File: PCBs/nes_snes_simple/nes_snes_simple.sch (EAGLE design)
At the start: 23 parts, among them IC1 74245

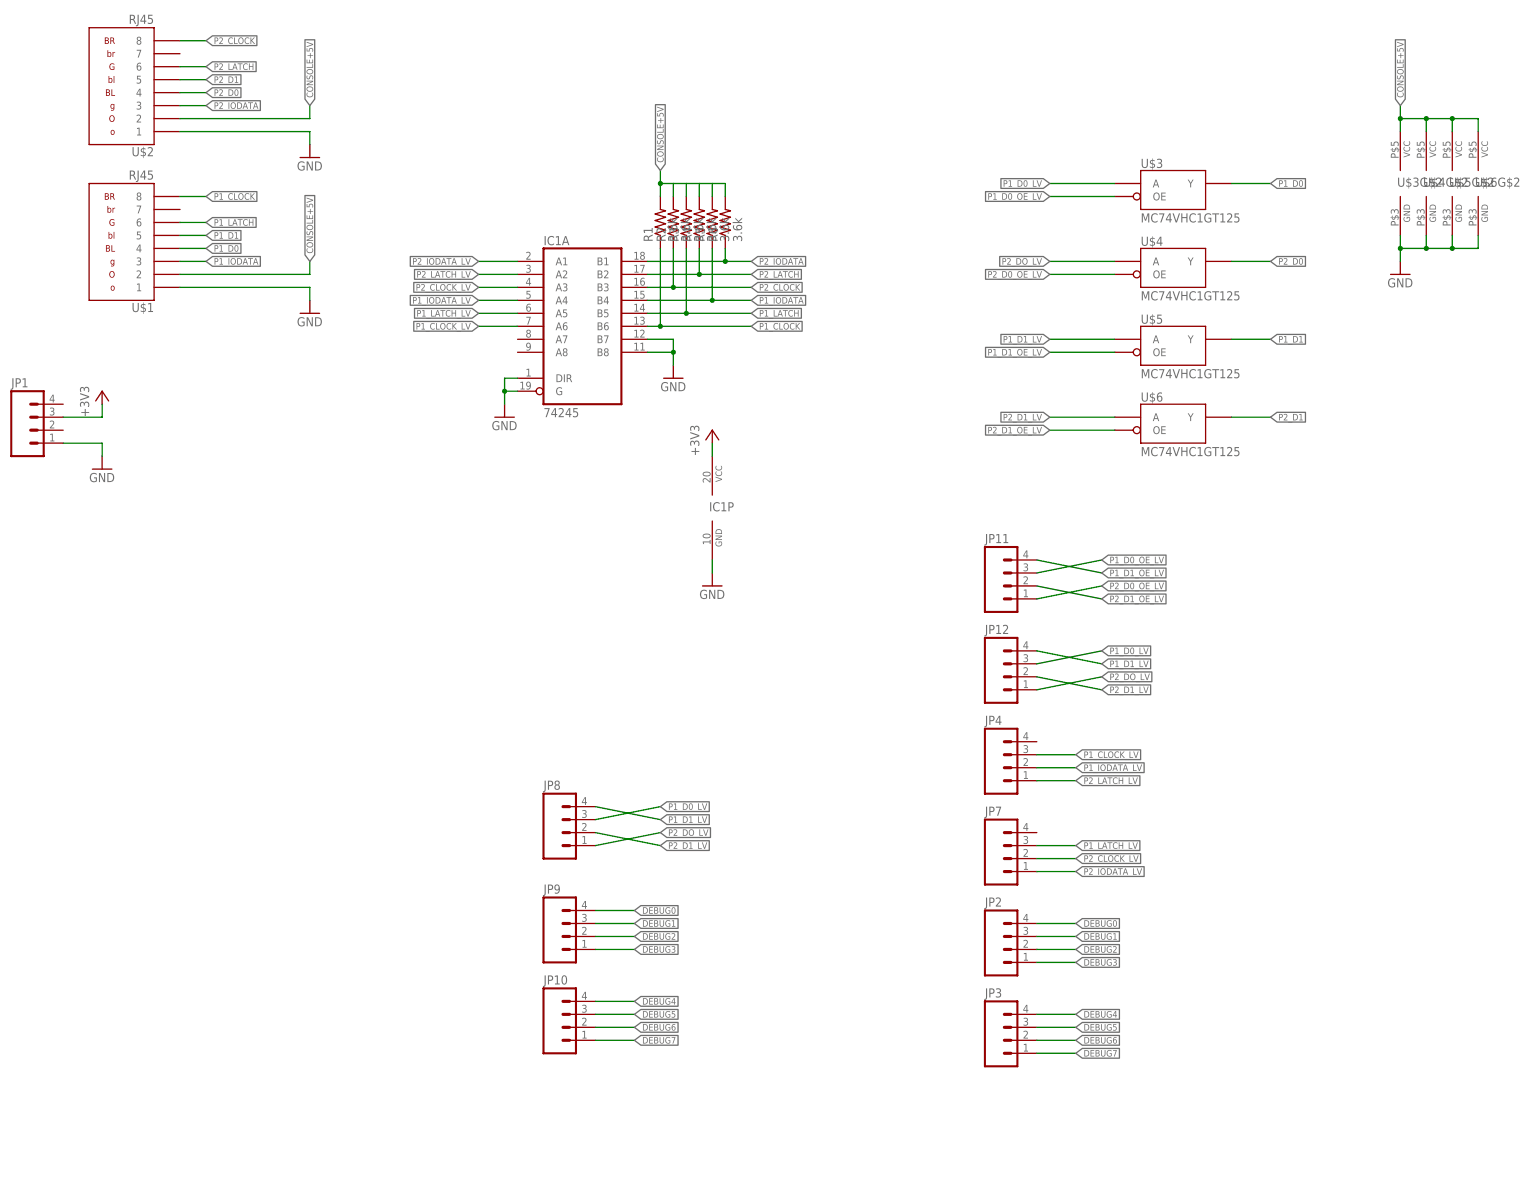
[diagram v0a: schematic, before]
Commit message: Added a tap for all the 5v lines from the console. Fixed part labels. Added more labeling. Added a logo. Cleaned up the schematic.
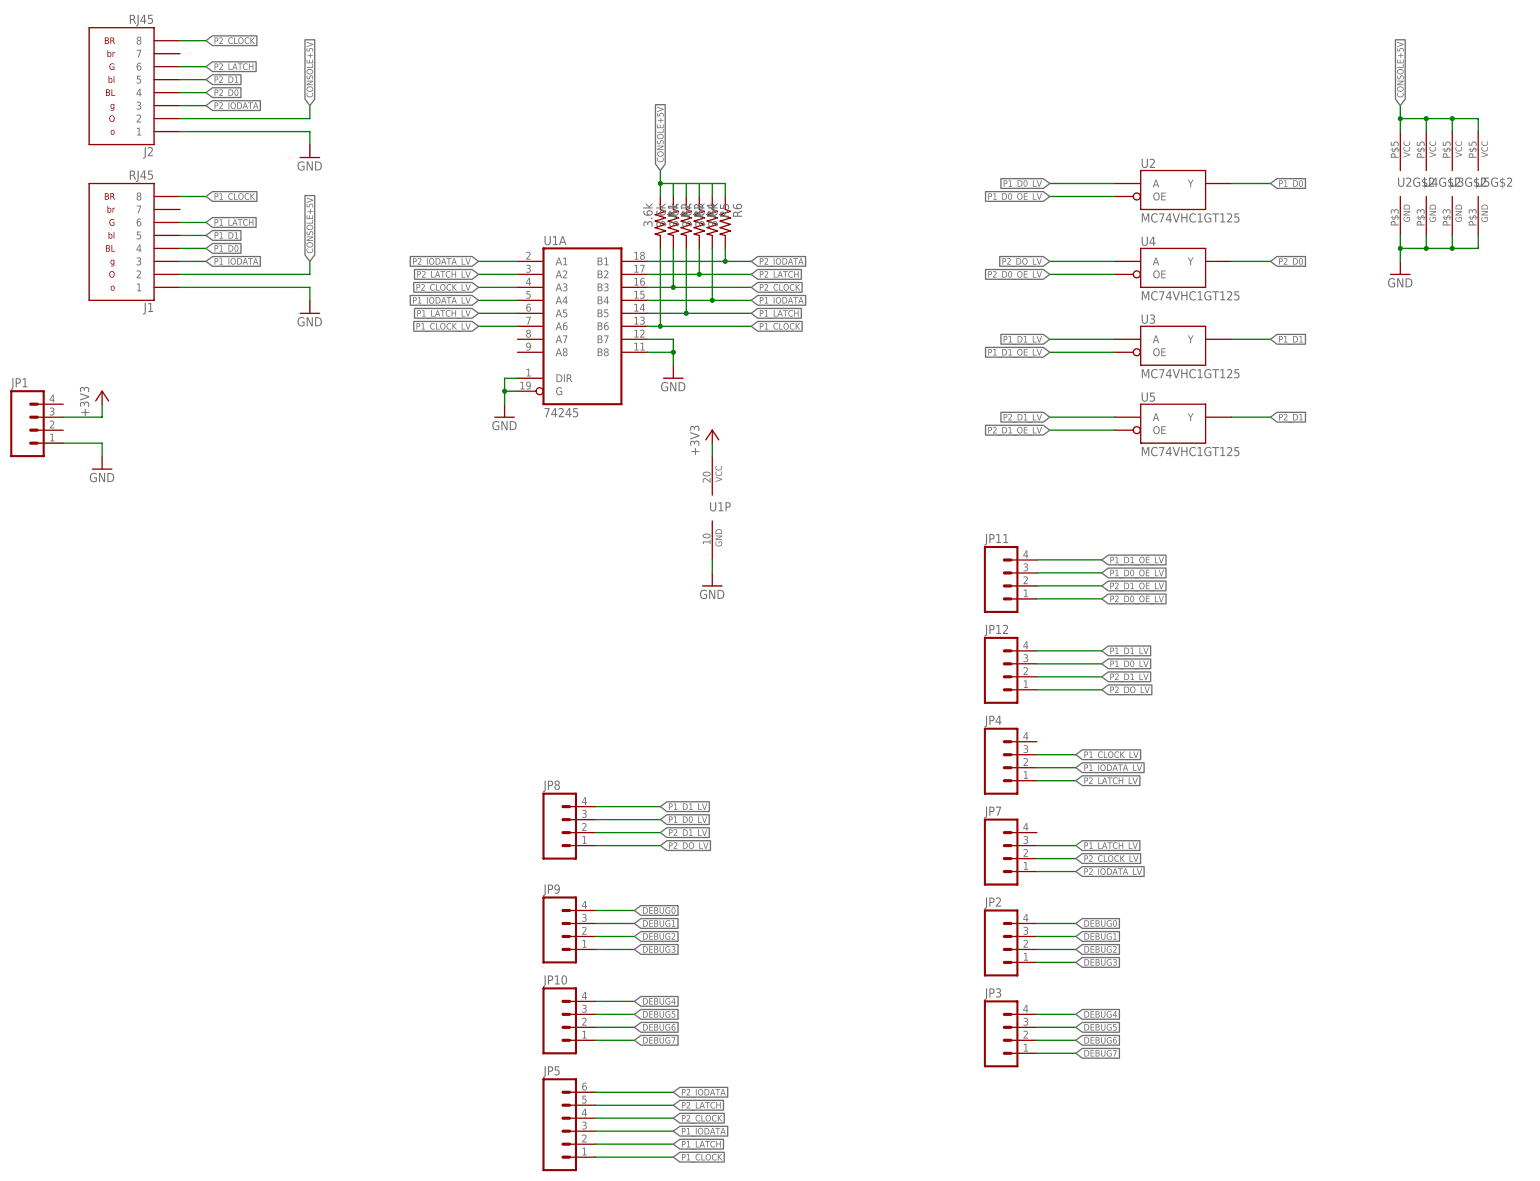
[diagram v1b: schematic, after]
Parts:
- added JP5: (no value), SparkFun-Connectors:M06SIP
- renumbered IC1 to U1, U$1 to J1, U$2 to J2, U$3 to U2, U$4 to U4, U$5 to U3, U$6 to U5
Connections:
- net CONSOLE+5V: now also R1.1, R2.1, R3.1, R4.1, R5.1, R6.1; no longer R1.2, R2.2, R3.2, R4.2, R5.2, R6.2
- net P1_CLOCK: now also JP5.1, R1.2; no longer R1.1
- net P1_IODATA: now also JP5.3, R5.2; no longer R5.1
- net P1_LATCH: now also JP5.2, R3.2; no longer R3.1
- net P2_CLOCK: now also JP5.4, R2.2; no longer R2.1
- net P2_IODATA: now also JP5.6, R6.2; no longer R6.1
- net P2_LATCH: now also JP5.5, R4.2; no longer R4.1
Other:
- moved on the sheet: R1, R2, R3, R4, R5, R6
